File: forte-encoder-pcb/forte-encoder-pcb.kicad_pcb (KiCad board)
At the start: 2 copper layers, 32.4 x 40 mm, 52 parts, among them CN3(OUT)1 XT30(2+2)PB-M.G.B, CN3(OUT)2 XT30(2+2)PB-M.G.B, J1 BM07B-SRSS-TB(LF)(SN), U2 STM32F103C8Tx, U3 MCP2542FD-E/MF, U4 MA732GQ-Z, U5 TPS629203DRLR, U6 TPS629203DRLR, Y1 CSTNE8M00G550000R0

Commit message: halp
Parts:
- removed CN1, CN2: ~, dash:xt-30
- removed CN3(OUT)2: XT30(2+2)PB-M.G.B, dash:XT30(2+2)PB-M.G.B
- added J10: Conn_01x01_Pin, TestPoint:TestPoint_Plated_Hole_D2.0mm, F.Cu at (94.2, 87.0)
- added J11: Conn_01x01_Pin, TestPoint:TestPoint_Plated_Hole_D2.0mm, F.Cu at (91.8, 88.2)
- added J6: Conn_01x01_Pin, TestPoint:TestPoint_Plated_Hole_D2.0mm, F.Cu at (86.5, 84.5)
- added J7: Conn_01x01_Pin, TestPoint:TestPoint_Plated_Hole_D2.0mm, F.Cu at (88.8, 83.3)
- added J8: Conn_01x01_Pin, TestPoint:TestPoint_Plated_Hole_D2.0mm, F.Cu at (91.2, 82.3)
- added J9: Conn_01x01_Pin, TestPoint:TestPoint_Plated_Hole_D2.0mm, F.Cu at (89.6, 89.5)
- C24, C28, C29, C30, C31, R10, R11, R12, U5, U6: moved to F.Cu
- C33, C35, C37, FL1, U3: moved to B.Cu
- moved CN3(OUT)1 52.1 mm to (114.2, 100.2), turned to -90 degrees
- moved C40 35.2 mm to (113.0, 89.7), turned to -90 degrees
- moved R13 33.0 mm to (106.0, 82.6), turned to 90 degrees
- moved C39 31.9 mm to (108.7, 84.8), turned to -90 degrees
- moved L2 30.3 mm to (106.7, 89.2), turned to -90 degrees
- moved C37 29.7 mm to (102.3, 81.1), turned to 0 degrees
- moved U6 29.7 mm to (107.9, 93.1), turned to 0 degrees
- moved R12 29.2 mm to (110.0, 92.9), turned to 90 degrees
- moved C38 28.4 mm to (96.4, 83.4), turned to -90 degrees
- moved VR1 28.1 mm to (101.1, 82.0), turned to 180 degrees
- moved C42 27.7 mm to (101.0, 85.3), turned to 0 degrees
- moved C43 27.7 mm to (102.2, 87.4), turned to 0 degrees
- moved R15 26.5 mm to (97.8, 86.0), turned to 0 degrees
- moved R14 25.2 mm to (106.3, 86.2), turned to -90 degrees
- moved U5 25.1 mm to (104.1, 92.3)
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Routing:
- net GND: track 0.00 -> 29.2 mm
- net +3.3V: track 0.00 -> 16.2 mm
- net +5V: track 0.00 -> 2.77 mm
- net Net-(U5-MODE/S-CONF): track 0.00 -> 2.70 mm
- net Net-(U2-VDDA): track 0.00 -> 1.86 mm
- net /INDICATOR: track 0.00 -> 1.75 mm
- net Net-(U5-FB/VSET): track 0.00 -> 1.38 mm
- net Net-(D2-Pad2): track 0.00 -> 1.38 mm
- net Net-(U6-MODE/S-CONF): track 0.00 -> 1.34 mm
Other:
- board size 32.4 x 40 mm -> 36.5 x 45 mm
- copper layers 2 -> 6

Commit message: modify pcb
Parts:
- C24, C28, L2, R11, R12, U5, U6: moved to B.Cu
- C38: moved to F.Cu
- moved J5 27.6 mm to (113.5, 89.9)
- moved R13 21.6 mm to (84.6, 84.8), turned to 130 degrees
- moved C33 21.1 mm to (95.8, 114.9), turned to 0 degrees
- moved D2 20.0 mm to (94.6, 121.6), turned to 0 degrees
- moved C54 18.5 mm to (95.8, 113.0), turned to 180 degrees
- moved R8 17.7 mm to (97.3, 121.6), turned to 180 degrees
- moved J4 16.9 mm to (108.1, 83.6)
- moved J3 16.9 mm to (111.0, 86.4)
- moved J1 15.9 mm to (104.6, 81.6)
- moved C37 15.9 mm to (86.7, 83.9), turned to 130 degrees
- moved J6 14.7 mm to (100.9, 80.2)
- moved U4 14.3 mm to (95.8, 110.0), turned to 0 degrees
- moved VR1 13.8 mm to (87.7, 85.1), turned to -50 degrees
- moved R14 11.4 mm to (95.2, 83.7), turned to -65 degrees
- moved FL1 10.4 mm to (101.3, 111.6)
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- renumbered J1 to J0, J7 to J1, J11 to J2, J10 to J3, J8 to J4, J6 to J5, J9 to J6
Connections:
- J1 pad 1: unconnected-(J7-Pin_1-Pad1) -> +48V
- J2 pad 1: unconnected-(J11-Pin_1-Pad1) -> +48V
- J3 pad 1: unconnected-(J10-Pin_1-Pad1) -> +48V
- J4 pad 1: unconnected-(J8-Pin_1-Pad1) -> GND
- J5 pad 1: unconnected-(J6-Pin_1-Pad1) -> GND
- J6 pad 1: unconnected-(J9-Pin_1-Pad1) -> GND
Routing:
- net GND: track 29.2 -> 0.00 mm
- net +3.3V: track 16.2 -> 0.00 mm
- net +5V: track 2.77 -> 0.00 mm
- net Net-(U5-MODE/S-CONF): track 2.70 -> 0.00 mm
- net Net-(U2-VDDA): track 1.86 -> 0.00 mm
- net /INDICATOR: track 1.75 -> 0.00 mm
- net Net-(U5-FB/VSET): track 1.38 -> 0.00 mm
- net Net-(D2-Pad2): track 1.38 -> 0.00 mm
- net Net-(U6-MODE/S-CONF): track 1.34 -> 0.00 mm

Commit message: super messy
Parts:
- added J10: Conn_01x01_Pin, TestPoint:TestPoint_THTPad_D1.5mm_Drill0.7mm, F.Cu at (110.2, 101.7)
- added J7: Conn_01x01_Pin, TestPoint:TestPoint_THTPad_D1.5mm_Drill0.7mm, F.Cu at (115.2, 108.3)
- added J8: Conn_01x01_Pin, TestPoint:TestPoint_THTPad_D1.5mm_Drill0.7mm, F.Cu at (110.2, 104.3)
- added J9: Conn_01x01_Pin, TestPoint:TestPoint_THTPad_D1.5mm_Drill0.7mm, F.Cu at (112.4, 108.3)
- FL1: moved to F.Cu
- moved TP11 42.9 mm to (151.6, 138.4)
- moved TP12 28.1 mm to (136.3, 135.9)
- moved TP14 24.8 mm to (131.2, 135.9)
- moved TP13 22.7 mm to (126.4, 135.8)
- moved D2 19.9 mm to (112.4, 112.6), turned to -90 degrees
- moved R8 14.8 mm to (110.4, 114.8), turned to 90 degrees
- moved C35 8.93 mm to (109.0, 106.6), turned to 180 degrees
- moved J2 4.73 mm to (92.2, 79.8)
- moved FL1 4.25 mm to (98.5, 108.5), turned to 15 degrees
- moved J6 3.53 mm to (97.4, 79.6)
- moved J1 2.02 mm to (102.8, 80.8)
- moved C29 1.22 mm to (107.9, 106.5)
- moved J4 1.15 mm to (107.2, 83.0)
- moved J0 0.92 mm to (88.8, 112.8)
- moved R10 0.73 mm to (98.0, 90.8)
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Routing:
- net GND: track 0.00 -> 115.0 mm, vias 0 -> 5
- net +5V: track 0.00 -> 49.3 mm, vias 0 -> 3
- net +48V: track 0.00 -> 44.4 mm, vias 0 -> 2
- net +3.3V: track 0.00 -> 26.8 mm, vias 1 -> 4
- net /TCK: track 0.00 -> 23.2 mm
- net /TMS: track 0.00 -> 20.1 mm, vias 0 -> 2
- net +12V: track 0.00 -> 18.6 mm, vias 0 -> 2
- net /NRST: track 0.00 -> 15.9 mm, vias 0 -> 2
- net /USART_TX: track 0.00 -> 12.6 mm, vias 0 -> 2
- net /CAN+: track 0.00 -> 10.3 mm
- net /CAN_RX: track 0.00 -> 9.97 mm, vias 0 -> 1
- net Net-(VR1-SW): track 0.00 -> 8.81 mm, vias 0 -> 1
- net /USART_RX: track 0.00 -> 8.34 mm
- net /CAN-: track 0.00 -> 7.32 mm
- net Net-(C42-Pad1): track 0.00 -> 7.19 mm
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- added copper zone on In2.Cu, net +3.3V
- added copper zone on In2.Cu, net +48V
- added copper zone on In1.Cu, net GND
- added copper zone on In4.Cu, net GND

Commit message: needa double check but "done"
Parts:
- moved TP_GND2 80.6 mm to (92.0, 83.1)
- moved TP_GND1 74.9 mm to (91.3, 91.5)
- moved TP2 64.0 mm to (103.8, 86.2)
- moved TP11 63.2 mm to (91.0, 120.4), turned to 180 degrees
- moved TP3 57.5 mm to (108.6, 91.2)
- moved TP4 55.9 mm to (105.0, 103.0)
- moved TP1 54.6 mm to (93.8, 90.8)
- moved TP12 45.8 mm to (93.0, 120.8), turned to 180 degrees
- moved TP13 43.5 mm to (92.8, 108.1), turned to 180 degrees
- moved TP14 39.0 mm to (95.1, 121.1), turned to 180 degrees
- moved C54 1.90 mm to (95.3, 114.8)
- moved C36 1.76 mm to (112.1, 112.5)
- moved U4 1.75 mm to (95.8, 111.8)
- moved C33 1.74 mm to (95.5, 116.6)
- moved R8 1.18 mm to (109.8, 115.8), turned to 0 degrees
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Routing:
- net +3.3V: track 26.8 -> 57.2 mm, vias 4 -> 7
- net /MOSI: track 0.00 -> 26.1 mm, vias 0 -> 2
- net /CS: track 0.00 -> 20.0 mm, vias 0 -> 2
- net /SCK: track 0.00 -> 14.7 mm, vias 0 -> 2
- net /MISO: track 0.00 -> 9.97 mm, vias 0 -> 2
- net /CAN+: track 10.3 -> 19.8 mm, vias 0 -> 1
- net GND: track 115.0 -> 124.5 mm, vias 5 -> 16
- net Net-(VR1-FB): track 3.16 -> 12.5 mm, vias 0 -> 2
- net /CAN-: track 7.32 -> 15.5 mm, vias 0 -> 1
- net +48V: track 44.4 -> 51.3 mm
- net +5V: track 49.3 -> 55.3 mm
- net Net-(VR1-RON): track 0.00 -> 3.79 mm, vias 0 -> 1
- net +12V: track 18.6 -> 22.3 mm
- net /USART_TX: track 12.6 -> 15.5 mm
- net /RCC_OSC_IN: track 0.00 -> 2.75 mm, vias 0 -> 1
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
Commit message: kcl shouldn't be an issue right...
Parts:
- added REF**: MountingHole_2.2mm_M2, MountingHole:MountingHole_2.2mm_M2, F.Cu at (109.0, 91.9)
- added REF**: MountingHole_2.2mm_M2, MountingHole:MountingHole_2.2mm_M2, F.Cu at (89.8, 120.0)
- moved TP14 7.19 mm to (102.0, 119.3)
- moved TP3 6.41 mm to (102.8, 88.5)
- moved TP12 5.16 mm to (98.1, 119.9)
- moved TP11 3.69 mm to (94.7, 121.1)
- moved J0 0.22 mm to (88.6, 112.8)
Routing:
- net +5V: track 55.3 -> 51.4 mm
- net /SCK: track 14.7 -> 13.3 mm
- net +3.3V: track 57.2 -> 56.6 mm

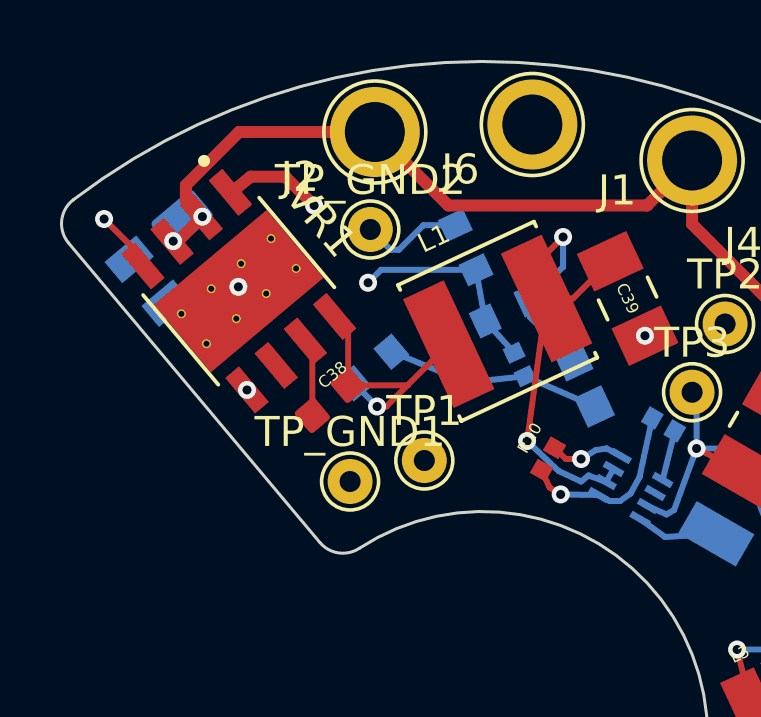
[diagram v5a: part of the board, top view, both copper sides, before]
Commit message: Mounting holes
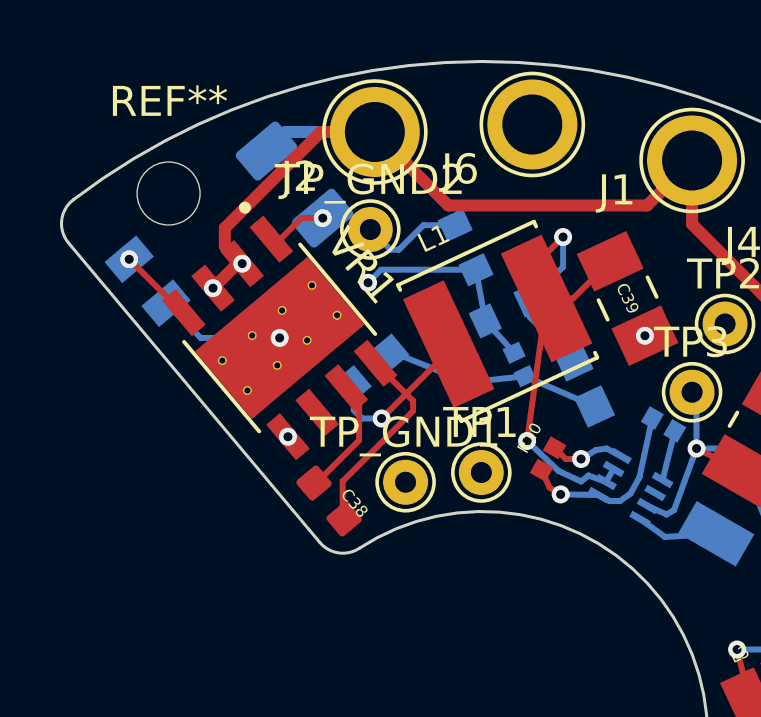
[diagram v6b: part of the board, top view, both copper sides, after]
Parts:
- added REF**: MountingHole_2.1mm, MountingHole:MountingHole_2.1mm, F.Cu at (85.3, 81.9)
- moved C37 3.63 mm to (89.5, 81.6)
- moved C38 3.36 mm to (90.7, 92.2), turned to -50 degrees
- moved VR1 2.07 mm to (89.0, 86.7)
- moved TP1 1.94 mm to (95.7, 91.2)
- moved TP_GND1 1.85 mm to (93.2, 91.5)
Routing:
- net +48V: track 51.3 -> 54.8 mm
- net Net-(VR1-SW): track 8.81 -> 12.2 mm
- net +12V: track 22.3 -> 20.5 mm
- net Net-(VR1-BST): track 2.57 -> 4.12 mm
- net Net-(VR1-RON): track 3.79 -> 2.56 mm
- net GND: track 124.5 -> 125.7 mm
- net Net-(VR1-FB): track 12.5 -> 13.2 mm
